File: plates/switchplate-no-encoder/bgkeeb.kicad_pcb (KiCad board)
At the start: 2 copper layers, 98.4 x 90.5 mm, 4 parts

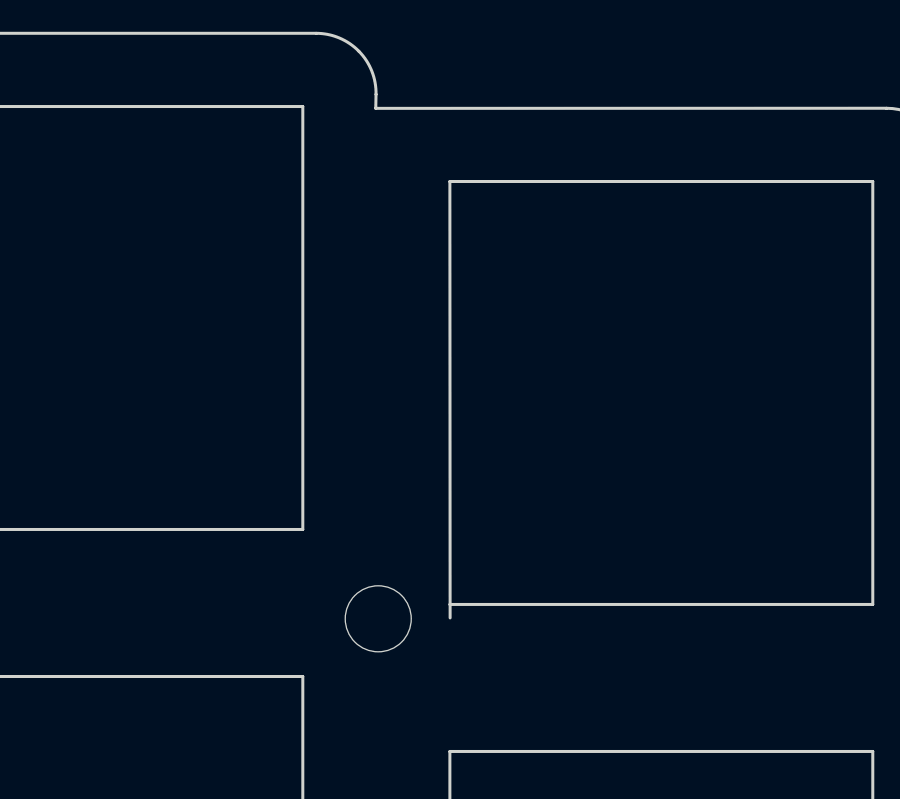
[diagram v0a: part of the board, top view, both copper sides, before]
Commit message: missed a switch hole line in my last commit
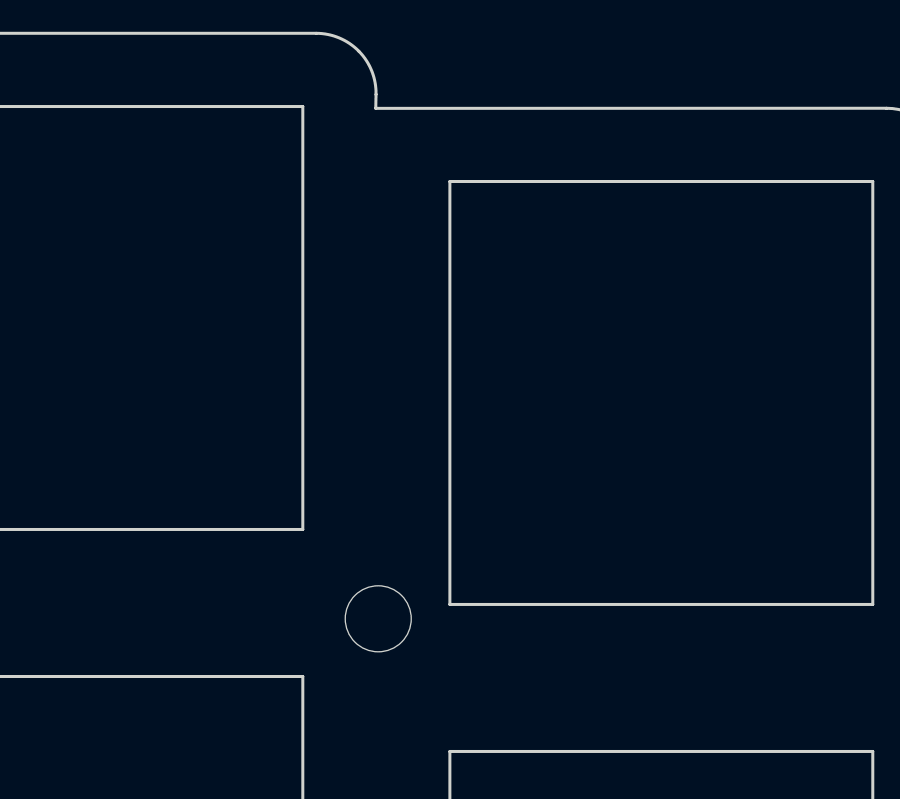
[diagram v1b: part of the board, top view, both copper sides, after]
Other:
- outline, holes or cut-outs redrawn
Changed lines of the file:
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@@
       (effects (font (size 1 1) (thickness 0.15)))
     )
+    (fp_circle (center 0 0) (end 2.45 0) (layer F.CrtYd) (width 0.05))
     (fp_circle (center 0 0) (end 2.2 0) (layer Cmts.User) (width 0.15))
-    (fp_circle (center 0 0) (end 2.45 0) (layer F.CrtYd) (width 0.05))
     (fp_text user %R (at 0.3 0) (layer F.Fab)
       (effects (font (size 1 1) (thickness 0.15)))
@@
       (effects (font (size 1 1) (thickness 0.15)))
     )
+    (fp_circle (center 0 0) (end 2.45 0) (layer F.CrtYd) (width 0.05))
     (fp_circle (center 0 0) (end 2.2 0) (layer Cmts.User) (width 0.15))
-    (fp_circle (center 0 0) (end 2.45 0) (layer F.CrtYd) (width 0.05))
     (fp_text user %R (at 0.3 0) (layer F.Fab)
       (effects (font (size 1 1) (thickness 0.15)))
@@
       (effects (font (size 1 1) (thickness 0.15)))
     )
+    (fp_circle (center 0 0) (end 2.45 0) (layer F.CrtYd) (width 0.05))
     (fp_circle (center 0 0) (end 2.2 0) (layer Cmts.User) (width 0.15))
-    (fp_circle (center 0 0) (end 2.45 0) (layer F.CrtYd) (width 0.05))
     (fp_text user %R (at 0.3 0) (layer F.Fab)
       (effects (font (size 1 1) (thickness 0.15)))
@@
       (effects (font (size 1 1) (thickness 0.15)))
     )
+    (fp_circle (center 0 0) (end 2.45 0) (layer F.CrtYd) (width 0.05))
     (fp_circle (center 0 0) (end 2.2 0) (layer Cmts.User) (width 0.15))
-    (fp_circle (center 0 0) (end 2.45 0) (layer F.CrtYd) (width 0.05))
     (fp_text user %R (at 0.3 0) (layer F.Fab)
       (effects (font (size 1 1) (thickness 0.15)))
@@
   (gr_line (start 129.952193 74.076204) (end 129.952193 59.974964) (layer Edge.Cuts) (width 0.1))
   (gr_line (start 144.049193 78.974164) (end 144.049193 93.075404) (layer Edge.Cuts) (width 0.1))
-  (gr_line (start 129.960233 55.524464) (end 129.952193 40.975764) (layer Edge.Cuts) (width 0.1))
+  (gr_line (start 129.952193 55.074464) (end 129.952193 40.975764) (layer Edge.Cuts) (width 0.1))
   (gr_line (start 91.953793 85.574784) (end 91.953793 71.476084) (layer Edge.Cuts) (width 0.1))
   (gr_line (start 91.953793 71.476084) (end 106.050793 71.476084) (layer Edge.Cuts) (width 0.1))
